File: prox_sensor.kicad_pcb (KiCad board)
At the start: 4 copper layers, 41.3 x 10.5 mm, 36 parts, among them J1 +, J10 GND, J2 -, J3 A, J5 3V3, J6 NRST, J7 SWCLK, J8 SWDIO, J9 K, U1 BD4840G-TR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

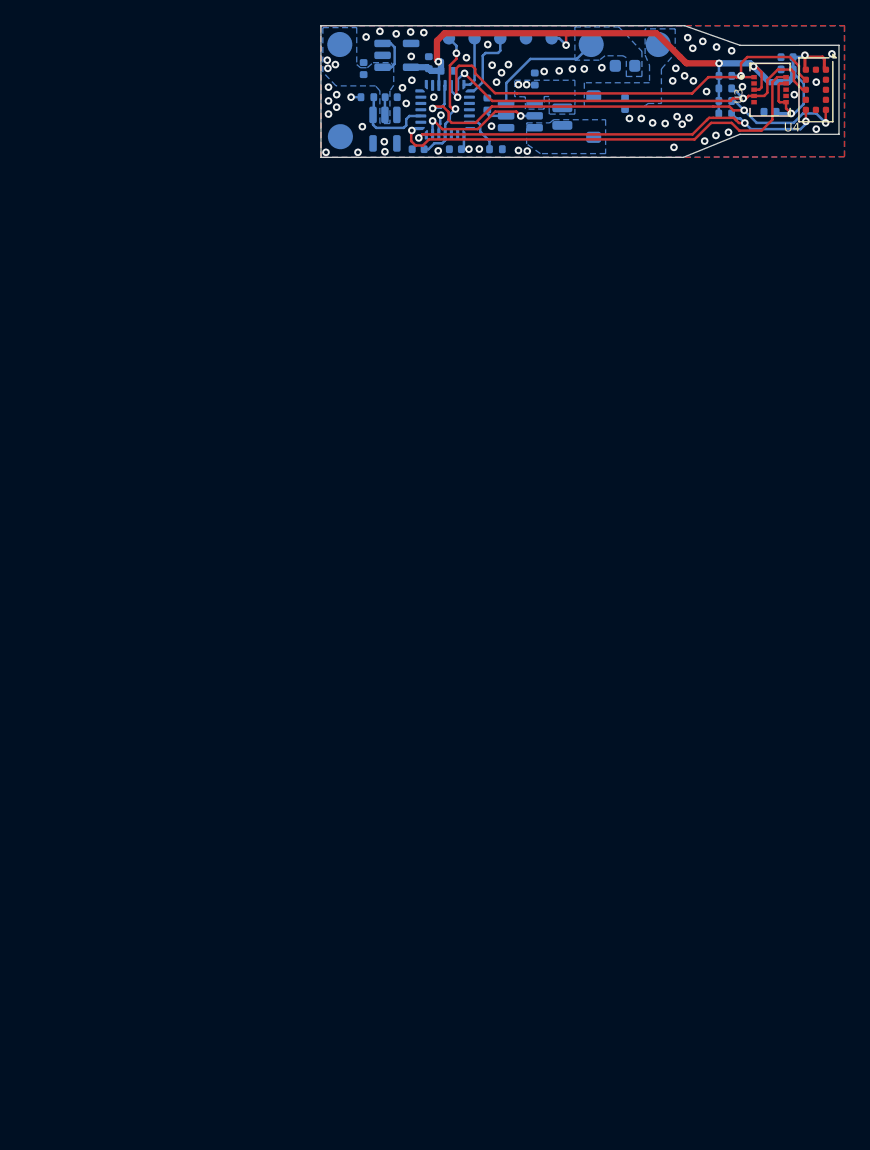
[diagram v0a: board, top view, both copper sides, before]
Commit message: Rev 4: separating sensors
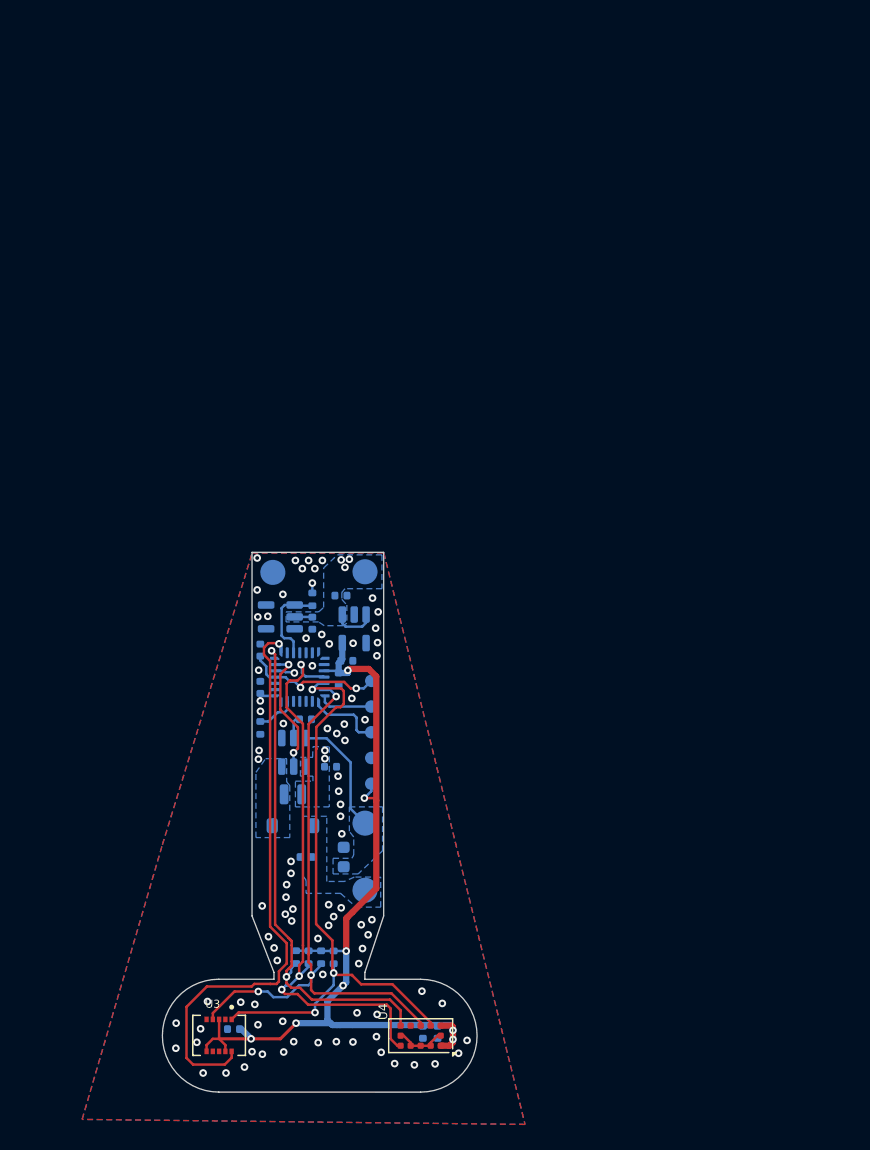
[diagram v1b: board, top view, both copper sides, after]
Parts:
- moved U3 87.3 mm to (137.7, 167.1), turned to -90 degrees
- moved C25 84.8 mm to (138.8, 166.6)
- moved C13 82.6 mm to (155.1, 166.8), turned to -90 degrees
- moved C16 82.1 mm to (153.9, 166.8), turned to 90 degrees
- moved U4 81.8 mm to (153.7, 167.1), turned to 180 degrees
- moved R18 76.9 mm to (146.8, 160.8), turned to 90 degrees
- moved R20 76.4 mm to (145.8, 160.8), turned to 90 degrees
- moved R2 75.9 mm to (144.8, 160.8), turned to 90 degrees
- moved R3 75.5 mm to (143.8, 160.8), turned to 90 degrees
- moved J3 71.4 mm to (149.3, 155.5), turned to 90 degrees
- moved R7 67.0 mm to (147.6, 152.8), turned to 90 degrees
- moved C20 65.3 mm to (144.6, 152.8), turned to 180 degrees
- moved J9 64.7 mm to (149.3, 150.1), turned to 90 degrees
- moved D1 61.4 mm to (143.6, 150.3), turned to 180 degrees
- moved J5 61.2 mm to (149.8, 147.0), turned to 180 degrees
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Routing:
- net /Mcu-unit: STM32/PA10_I2C_SDA: track 33.3 -> 47.3 mm, vias 2 -> 3
- net /Mcu-unit: STM32/PA9_I2C_SCL: track 37.6 -> 49.0 mm, vias 2 -> 3
- net +3V3: track 67.9 -> 79.0 mm, vias 9 -> 11
- net /Mcu-unit: STM32/PA2_STH_GPIO_INT: track 36.2 -> 46.6 mm
- net /Mcu-unit: STM32/PA8_ToF_XSHUT: track 39.0 -> 45.0 mm
- net /Mcu-unit: STM32/PA1_ToF_GPIO: track 35.3 -> 40.6 mm, vias 3 -> 2
- net GND: track 0.00 -> 4.16 mm, vias 62 -> 88
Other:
- board size 41.3 x 10.5 mm -> 25.1 x 43 mm
- board text added: "Frosted Ring"
- board text added: "Mirror Area"
- board text added: "d=130mm"
- board text added: "d=154mm"
- board text added: "d=9mm"
- board text added: "hole"
- board text added: "l=16mm"
- board text added: "l=70.5mm"

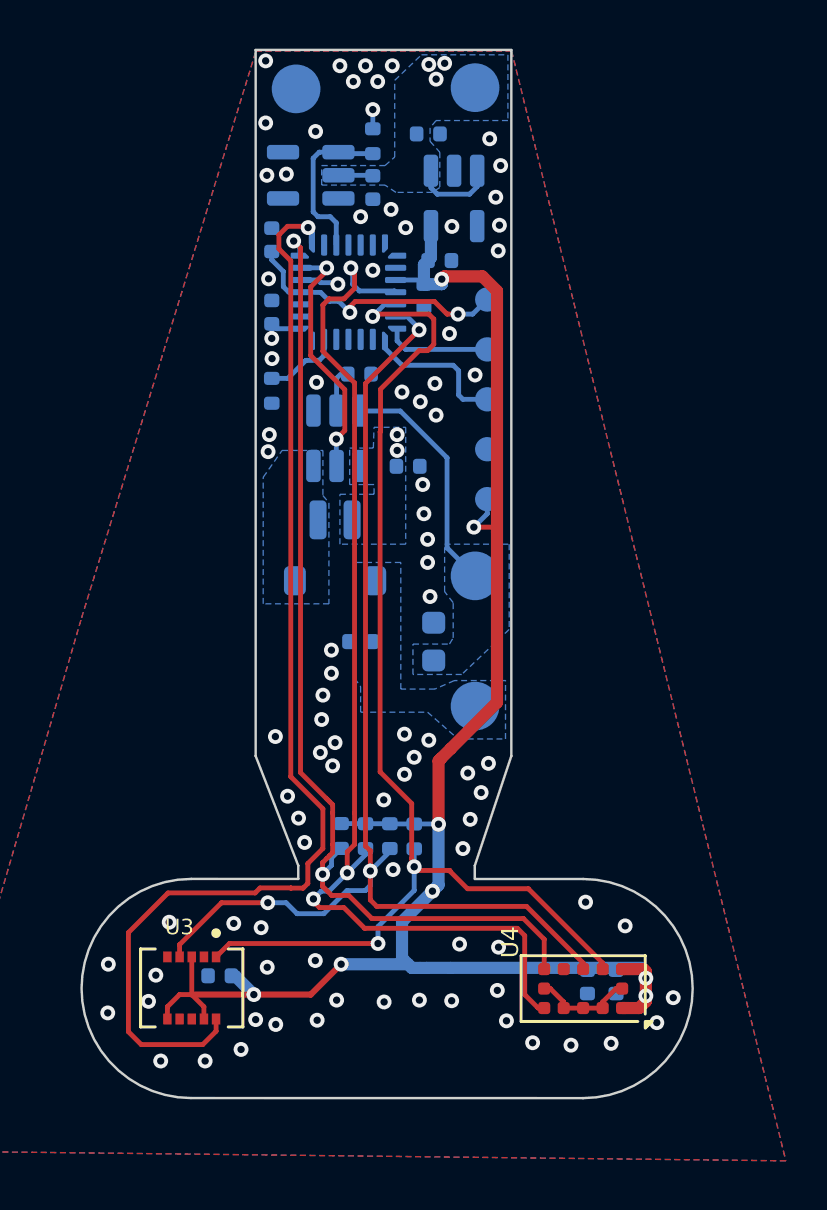
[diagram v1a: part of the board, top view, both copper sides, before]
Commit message: Separate sensors, refactoring
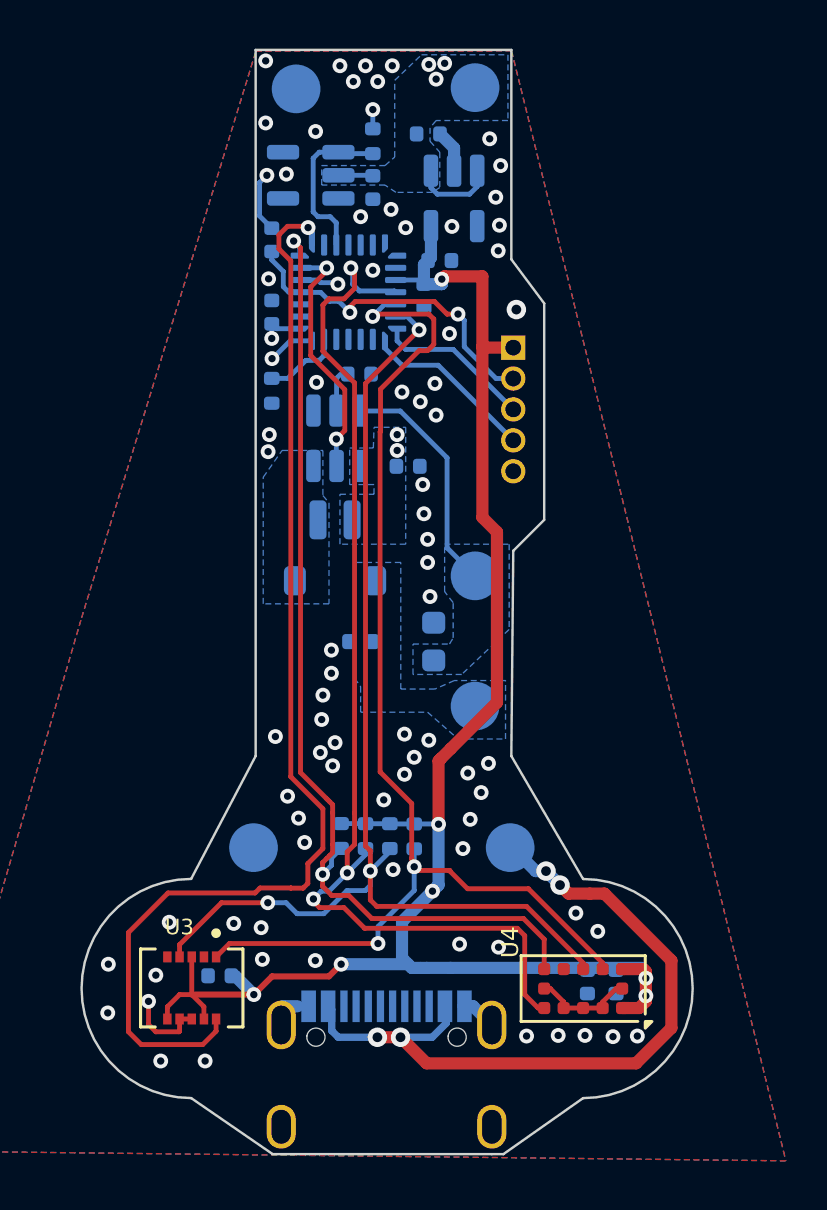
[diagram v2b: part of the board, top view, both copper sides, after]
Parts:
- removed J10: GND, TestPoint:TestPoint_Pad_D1.0mm
- removed J5: 3V3, TestPoint:TestPoint_Pad_D1.0mm
- removed J6: NRST, TestPoint:TestPoint_Pad_D1.0mm
- removed J7: SWCLK, TestPoint:TestPoint_Pad_D1.0mm
- removed J8: SWDIO, TestPoint:TestPoint_Pad_D1.0mm
- added J12: Conn_01x05, Connector_PinHeader_1.27mm:PinHeader_1x05_P1.27mm_Vertical, B.Cu at (150.9, 140.8)
- added USBC1: ~, 1-COB-MOD:USB-C_SMD-TYPE-C-31-M-12, B.Cu at (145.7, 170.3)
- added gnd: -, TestPoint:TestPoint_Pad_D2.0mm, B.Cu at (140.2, 161.3)
- added vusb: -, TestPoint:TestPoint_Pad_D2.0mm, B.Cu at (150.7, 161.3)
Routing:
- net Net-(J4-Pin_1): track 0.00 -> 30.0 mm, vias 0 -> 4
- net GND: track 4.16 -> 16.6 mm, vias 88 -> 78
- net /Mcu-unit: STM32/NRST: track 11.2 -> 13.8 mm
- net /Mcu-unit: STM32/SWDIO: track 4.35 -> 6.44 mm
- net /Mcu-unit: STM32/SWCLK: track 5.96 -> 7.14 mm
- net +3V3: track 79.0 -> 78.1 mm, vias 11 -> 10
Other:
- board size 25.1 x 43 mm -> 25.1 x 45.3 mm

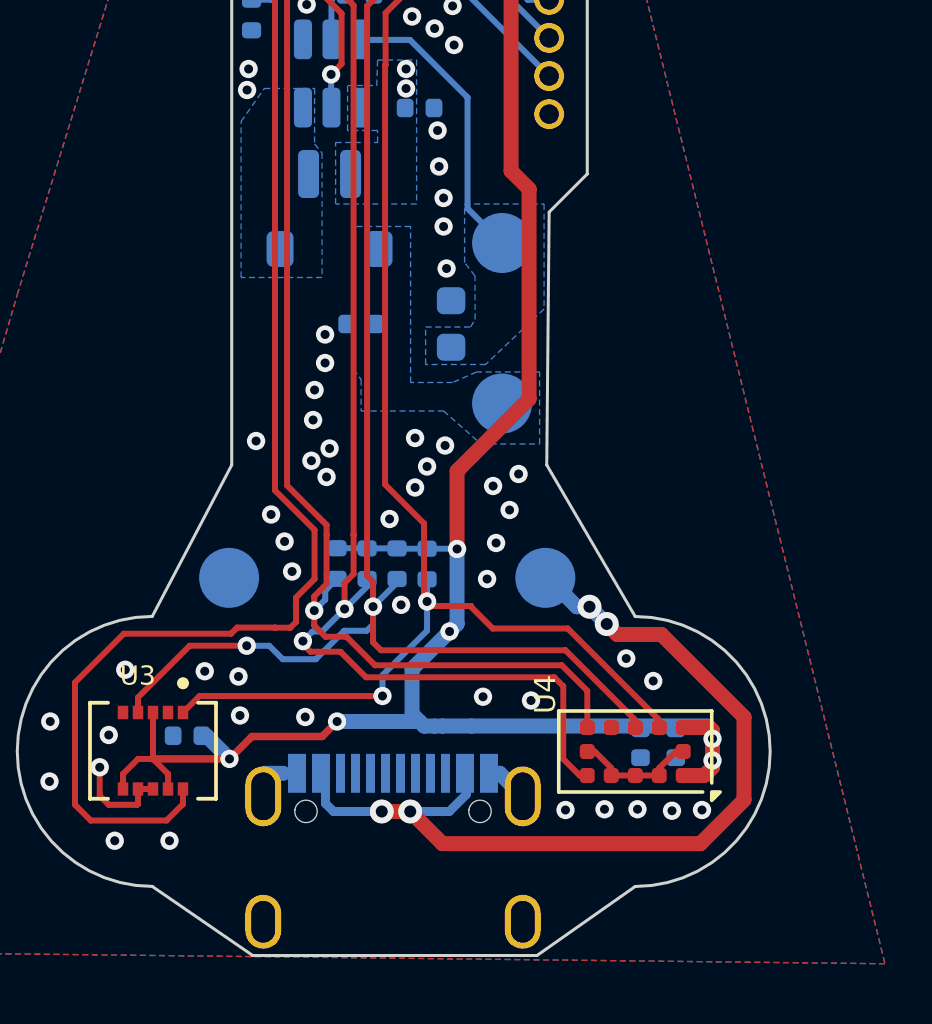
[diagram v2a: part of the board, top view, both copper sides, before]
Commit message: Adding light sensor
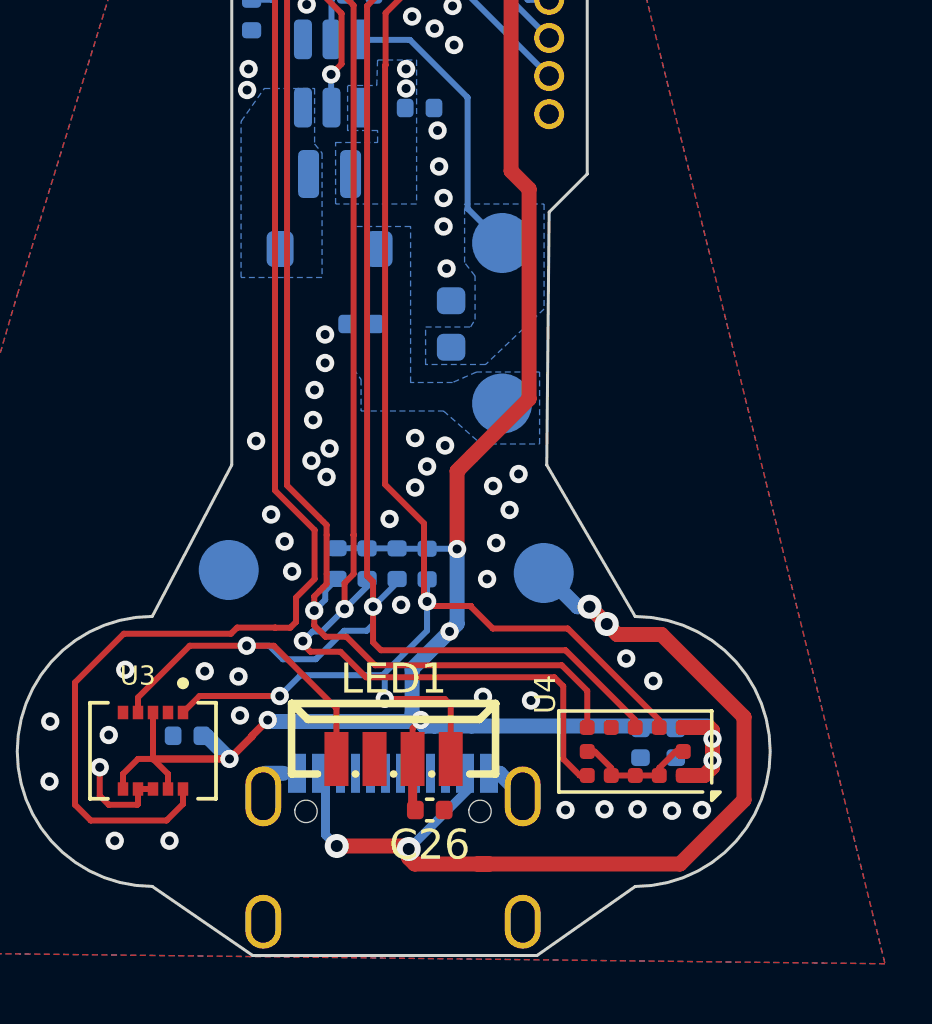
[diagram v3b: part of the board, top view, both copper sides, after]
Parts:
- removed gnd, vusb: -, TestPoint:TestPoint_Pad_D2.0mm
- added C26: 100nF/16V, Capacitor_SMD:C_0402_1005Metric, F.Cu at (146.9, 169.0)
- added GND1: -, TestPoint:TestPoint_Pad_D2.0mm, B.Cu at (140.2, 161.0)
- added LED1: ~, 1-COB-MOD:LED-SMD_4P-L6.8-W2.4_VEML7700-TR, F.Cu at (145.7, 167.3)
- added VBUS1: -, TestPoint:TestPoint_Pad_D2.0mm, B.Cu at (150.7, 161.1)
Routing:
- net /Mcu-unit: STM32/PA10_I2C_SDA: track 47.3 -> 52.8 mm
- net /Mcu-unit: STM32/PA9_I2C_SCL: track 49.0 -> 53.5 mm, vias 3 -> 4
- net Net-(VBUS1-Pin_1): track 30.0 -> 33.2 mm
- net +3V3: track 78.1 -> 81.1 mm, vias 10 -> 11
- net GND: vias 78 -> 77

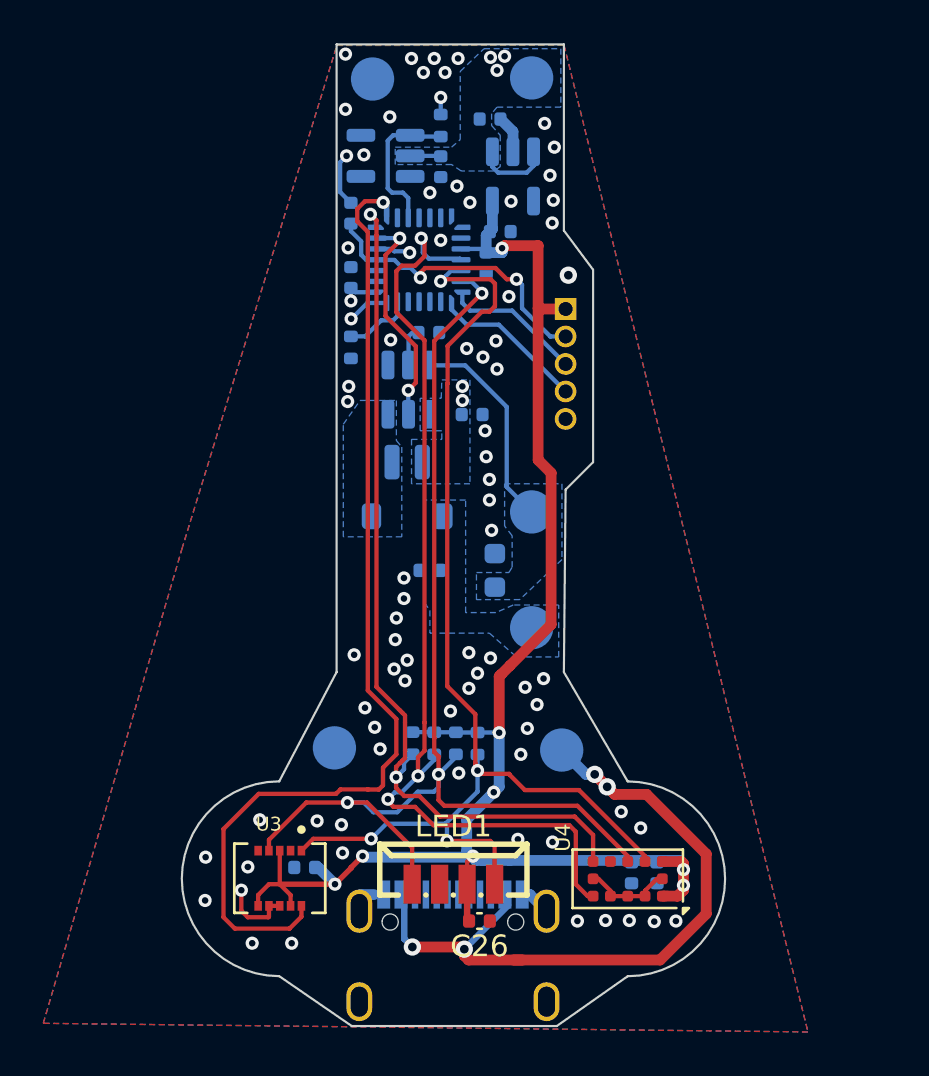
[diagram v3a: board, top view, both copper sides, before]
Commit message: swdio connector
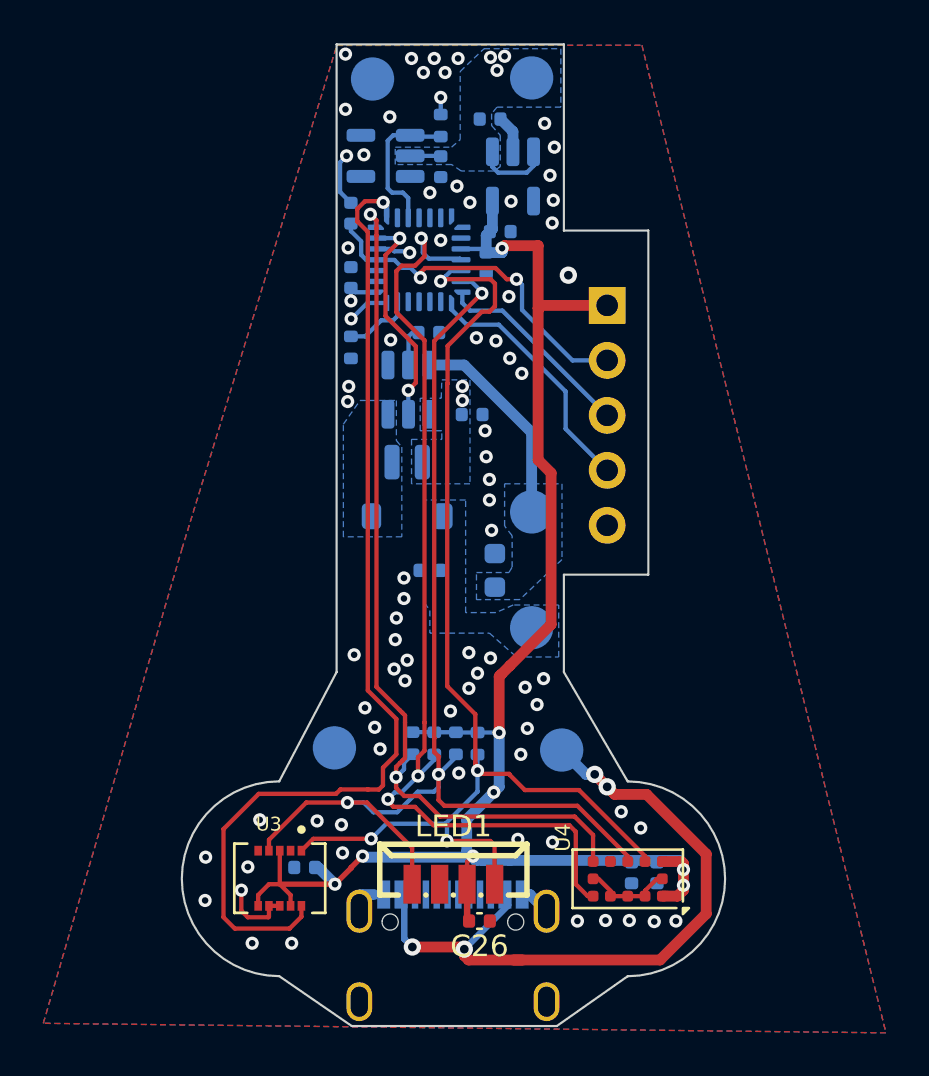
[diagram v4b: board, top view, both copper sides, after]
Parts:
- J12: footprint Connector_PinHeader_1.27mm:PinHeader_1x05_P1.27mm_Vertical -> Connector_PinHeader_2.54mm:PinHeader_1x05_P2.54mm_Vertical
- moved J12 1.93 mm to (152.8, 140.6)
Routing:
- net /Mcu-unit: STM32/SWCLK: track 7.14 -> 11.6 mm
- net /Mcu-unit: STM32/SWDIO: track 6.44 -> 9.34 mm
- net /Mcu-unit: STM32/NRST: track 13.8 -> 16.2 mm
- net +3V3: track 81.1 -> 83.1 mm
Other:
- outline, holes or cut-outs redrawn
